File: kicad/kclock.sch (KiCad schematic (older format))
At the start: 0 parts

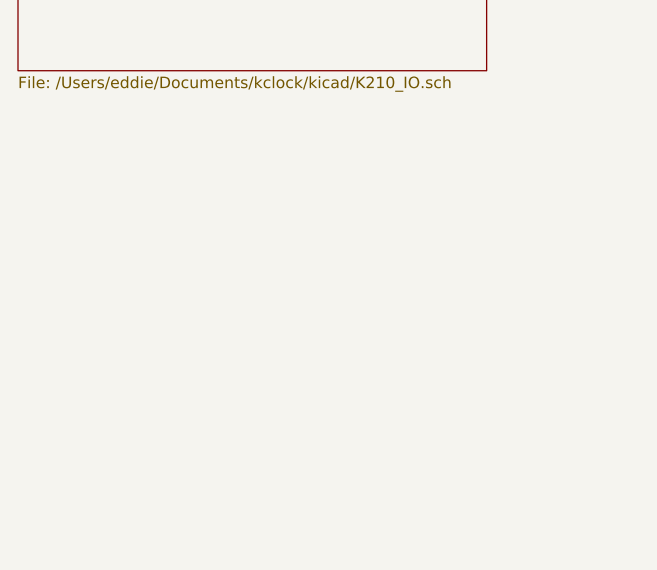
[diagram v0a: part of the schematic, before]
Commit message: ESP32 added to schematic. ESP32 refs. Slight mod to block diagram.
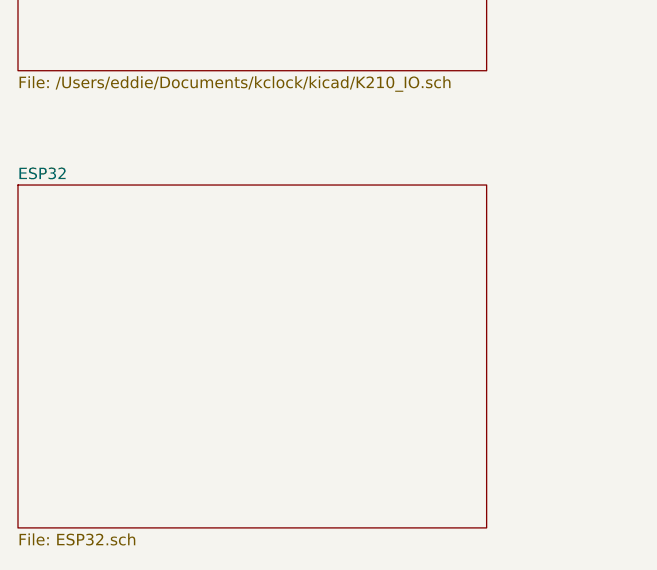
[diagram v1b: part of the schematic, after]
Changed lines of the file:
@@
 $Descr A4 11693 8268
 encoding utf-8
-Sheet 1 3
+Sheet 1 4
 Title ""
 Date ""
@@
 F1 "/Users/eddie/Documents/kclock/kicad/K210_Power.sch" 50
 $EndSheet
+$Sheet
+S 2000 5500 2050 1500
+U 5E91F1DB
+F0 "ESP32" 50
+F1 "ESP32.sch" 50
+$EndSheet
 $EndSCHEMATC

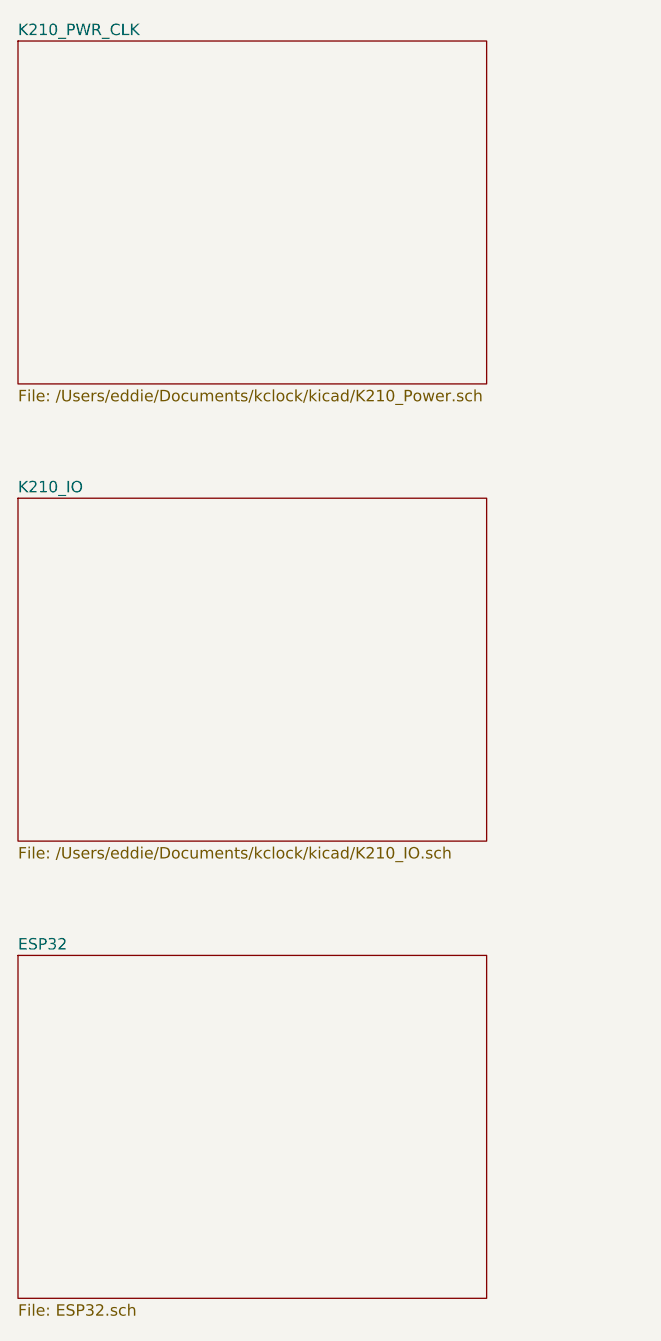
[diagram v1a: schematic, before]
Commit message: 3 output SMPS added MIC23450
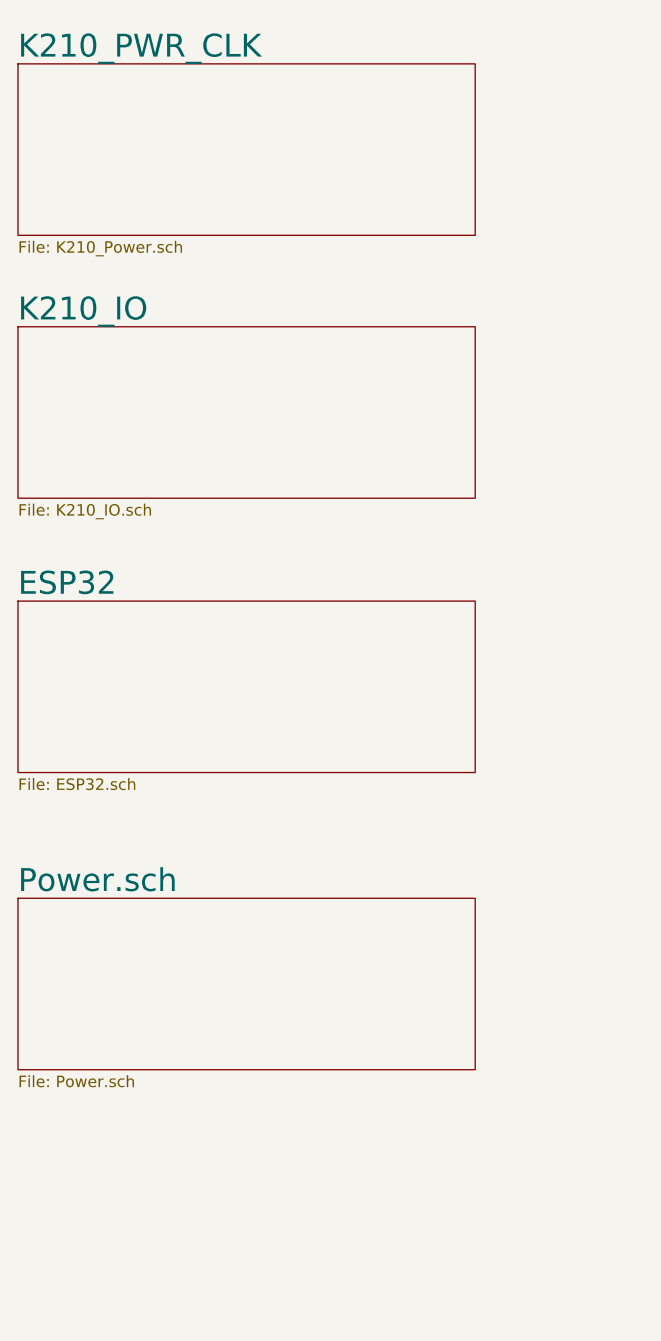
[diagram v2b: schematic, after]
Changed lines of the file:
@@
 $Descr A4 11693 8268
 encoding utf-8
-Sheet 1 4
+Sheet 1 5
 Title ""
 Date ""
@@
 $EndDescr
 $Sheet
-S 2000 3500 2050 1500
-U 5E870119
-F0 "K210_IO" 50
-F1 "/Users/eddie/Documents/kclock/kicad/K210_IO.sch" 50
+S 2000 5250 2000 750
+U 5E96F600
+F0 "Power.sch" 100
+F1 "Power.sch" 50
 $EndSheet
 $Sheet
-S 2000 1500 2050 1500
+S 2000 1600 2000 750
 U 5E86EC11
-F0 "K210_PWR_CLK" 50
-F1 "/Users/eddie/Documents/kclock/kicad/K210_Power.sch" 50
+F0 "K210_PWR_CLK" 100
+F1 "K210_Power.sch" 50
 $EndSheet
 $Sheet
-S 2000 5500 2050 1500
+S 2000 2750 2000 750
+U 5E870119
+F0 "K210_IO" 100
+F1 "K210_IO.sch" 50
+$EndSheet
+$Sheet
+S 2000 3950 2000 750
 U 5E91F1DB
-F0 "ESP32" 50
+F0 "ESP32" 100
 F1 "ESP32.sch" 50
 $EndSheet
